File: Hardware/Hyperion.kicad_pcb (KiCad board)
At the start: 2 copper layers, 90.2 x 95.9 mm, 1 part, among them J1 CUBESAT-BUS

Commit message: Add core components
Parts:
- added C1: 3.3uF, CAPC1608, F.Cu at (152.4, 87.6)
- added C10: 1000pF, CAPC1608, F.Cu at (141.0, 97.2)
- added C11: 0.1uF, CAPC1608, F.Cu at (139.1, 97.2)
- added C2: 0.1uF, CAPC1608, F.Cu at (141.0, 94.0)
- added C3: 0.1uF, CAPC1608, F.Cu at (141.0, 102.9)
- added C4: 0.1uF, CAPC1608, F.Cu at (149.2, 110.5)
- added C5: 0.1uF, CAPC1608, F.Cu at (155.6, 110.5)
- added C6: 0.1uF, CAPC1608, F.Cu at (163.8, 102.2)
- added C7: 0.1uF, CAPC1608, F.Cu at (163.8, 97.8)
- added C8: 0.1uF, CAPC1608, F.Cu at (155.6, 87.6)
- added C9: 0.1uF, CAPC1608, F.Cu at (149.2, 87.6)
- added FB1: 10, INDC1608, F.Cu at (139.1, 94.0)
- added U1: TM4C123GH6PZ, QFP50P1600X1600-100N, F.Cu at (152.4, 99.1)
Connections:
- J1 pad 1.1: N-0000092 -> (no net)
- J1 pad 1.10: N-0000070 -> (no net)
- J1 pad 1.11: N-0000065 -> (no net)
- J1 pad 1.12: N-0000060 -> (no net)
- J1 pad 1.13: N-0000055 -> (no net)
- J1 pad 1.14: N-00000103 -> (no net)
- J1 pad 1.15: N-0000099 -> (no net)
- J1 pad 1.16: N-0000095 -> (no net)
- J1 pad 1.17: N-0000091 -> (no net)
- J1 pad 1.18: N-0000087 -> (no net)
- J1 pad 1.19: N-0000083 -> (no net)
- J1 pad 1.2: N-0000078 -> (no net)
- J1 pad 1.20: N-0000069 -> (no net)
- J1 pad 1.21: N-0000064 -> (no net)
- J1 pad 1.22: N-0000059 -> (no net)
- J1 pad 1.23: N-0000054 -> (no net)
- J1 pad 1.24: N-00000102 -> (no net)
- J1 pad 1.25: N-0000098 -> (no net)
- J1 pad 1.26: N-0000094 -> (no net)
- J1 pad 1.27: N-0000090 -> (no net)
- J1 pad 1.28: N-0000086 -> (no net)
- J1 pad 1.29: N-0000082 -> (no net)
- J1 pad 1.3: N-0000077 -> (no net)
- J1 pad 1.30: N-0000068 -> (no net)
- J1 pad 1.31: N-0000063 -> (no net)
- J1 pad 1.32: N-0000058 -> (no net)
- J1 pad 1.33: N-0000066 -> (no net)
- J1 pad 1.34: N-00000101 -> (no net)
- J1 pad 1.35: N-0000097 -> (no net)
- J1 pad 1.36: N-0000093 -> (no net)
- J1 pad 1.37: N-0000089 -> (no net)
- J1 pad 1.38: N-0000085 -> (no net)
- J1 pad 1.39: N-0000081 -> (no net)
- J1 pad 1.4: N-0000076 -> (no net)
- J1 pad 1.40: N-0000067 -> (no net)
- J1 pad 1.41: N-0000062 -> (no net)
- J1 pad 1.42: N-0000057 -> (no net)
- J1 pad 1.43: N-00000104 -> (no net)
- J1 pad 1.44: N-00000100 -> (no net)
- J1 pad 1.45: N-0000096 -> (no net)
- J1 pad 1.46: N-0000079 -> (no net)
- J1 pad 1.47: N-0000088 -> (no net)
- J1 pad 1.48: N-0000084 -> (no net)
- J1 pad 1.49: N-0000080 -> (no net)
- J1 pad 1.5: N-0000075 -> (no net)
- J1 pad 1.50: N-0000053 -> (no net)
- J1 pad 1.51: N-0000061 -> (no net)
- J1 pad 1.52: N-0000056 -> (no net)
- J1 pad 1.6: N-0000074 -> (no net)
- J1 pad 1.7: N-0000073 -> (no net)
- J1 pad 1.8: N-0000072 -> (no net)
- J1 pad 1.9: N-0000071 -> (no net)
- J1 pad 2.1: N-0000040 -> (no net)
- J1 pad 2.10: N-0000018 -> (no net)
- J1 pad 2.11: N-0000013 -> (no net)
- J1 pad 2.12: N-000008 -> (no net)
- J1 pad 2.13: N-000003 -> (no net)
- J1 pad 2.14: N-0000051 -> (no net)
- J1 pad 2.15: N-0000047 -> (no net)
- J1 pad 2.16: N-0000043 -> (no net)
- J1 pad 2.17: N-0000039 -> (no net)
- J1 pad 2.18: N-0000035 -> (no net)
- J1 pad 2.19: N-0000031 -> (no net)
- J1 pad 2.2: N-0000026 -> (no net)
- J1 pad 2.20: N-0000017 -> (no net)
- J1 pad 2.21: N-0000012 -> (no net)
- J1 pad 2.22: N-000007 -> (no net)
- J1 pad 2.23: N-000002 -> (no net)
- J1 pad 2.24: N-0000050 -> (no net)
- J1 pad 2.25: N-0000046 -> (no net)
- J1 pad 2.26: N-0000042 -> (no net)
- J1 pad 2.27: N-0000038 -> (no net)
- J1 pad 2.28: N-0000034 -> (no net)
- J1 pad 2.29: N-0000030 -> (no net)
- J1 pad 2.3: N-0000025 -> (no net)
- J1 pad 2.30: N-0000016 -> (no net)
- J1 pad 2.31: N-0000011 -> (no net)
- J1 pad 2.32: N-000006 -> (no net)
- J1 pad 2.33: N-0000014 -> (no net)
- J1 pad 2.34: N-0000049 -> (no net)
- J1 pad 2.35: N-0000045 -> (no net)
- J1 pad 2.36: N-0000041 -> (no net)
- J1 pad 2.37: N-0000037 -> (no net)
- J1 pad 2.38: N-0000033 -> (no net)
- J1 pad 2.39: N-0000029 -> (no net)
- J1 pad 2.4: N-0000024 -> (no net)
- J1 pad 2.40: N-0000015 -> (no net)
- J1 pad 2.41: N-0000010 -> (no net)
- J1 pad 2.42: N-000005 -> (no net)
- J1 pad 2.43: N-0000052 -> (no net)
- J1 pad 2.44: N-0000048 -> (no net)
- J1 pad 2.45: N-0000044 -> (no net)
- J1 pad 2.46: N-0000027 -> (no net)
- J1 pad 2.47: N-0000036 -> (no net)
- J1 pad 2.48: N-0000032 -> (no net)
- J1 pad 2.49: N-0000028 -> (no net)
- J1 pad 2.5: N-0000023 -> (no net)
- J1 pad 2.50: N-000001 -> (no net)
- J1 pad 2.51: N-000009 -> (no net)
- J1 pad 2.52: N-000004 -> (no net)
- J1 pad 2.6: N-0000022 -> (no net)
- J1 pad 2.7: N-0000021 -> (no net)
- J1 pad 2.8: N-0000020 -> (no net)
- J1 pad 2.9: N-0000019 -> (no net)

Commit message: Core layout
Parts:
- added C12: 0.1uF, CAPC1005-N, F.Cu at (153.8, 113.2)
- added C13: 0.1uF, CAPC1005-N, F.Cu at (158.2, 92.2)
- added C14: 0.1uF, CAPC1005-N, F.Cu at (150.2, 92.2)
- added C15: C, CAPC1005-N, F.Cu at (155.0, 86.8)
- added C16: 0.1uF, CAPC1005-N, F.Cu at (145.2, 98.2)
- added C17: C, CAPC1005-N, F.Cu at (152.5, 86.8)
- added C18: 0.1uF, CAPC1005-N, F.Cu at (145.2, 104.8)
- added R1: 1k, RESC1005-N, F.Cu at (157.0, 86.0)
- added R2: R, RESC1005-N, F.Cu at (152.5, 92.2)
- added X1: 32.768kHz, XTAL-2SMD-32x15, F.Cu at (160.0, 89.5)
- added X2: 16MHz, XTAL-2SMD-50X32, F.Cu at (153.8, 89.5)
- C1: value 3.3uF -> 0.1uF; footprint CAPC1608 -> CAPC1005-N
- C10: value 1000pF -> 0.1uF; footprint CAPC1608 -> CAPC1005-N
- C11, C8: value 0.1uF -> 20pF; footprint CAPC1608 -> CAPC1005-N
- C2, C3, C4, C5, C7: footprint CAPC1608 -> CAPC1005-N
- C6: value 0.1uF -> 3.3uF; footprint CAPC1608 -> CAPC1005-N
- C9: value 0.1uF -> 1000pF; footprint CAPC1608 -> CAPC1005-N
- FB1: footprint INDC1608 -> INDC1005-N
- moved C9 24.5 mm to (153.8, 111.8), turned to 0 degrees
- moved C10 23.8 mm to (164.8, 98.8), turned to 90 degrees
- moved FB1 22.8 mm to (151.2, 113.2), turned to 180 degrees
- moved C11 22.3 mm to (158.8, 86.8), turned to 0 degrees
- moved C2 20.5 mm to (151.2, 111.8), turned to 0 degrees
- moved C6 20.1 mm to (143.8, 101.2), turned to 270 degrees
- moved C1 18.8 mm to (164.8, 101.8), turned to 90 degrees
- moved C3 18.2 mm to (155.8, 92.2), turned to 180 degrees
- moved C4 10.1 mm to (145.2, 101.2), turned to 270 degrees
- moved C7 7.02 mm to (164.8, 104.8), turned to 90 degrees
- moved C8 5.74 mm to (161.2, 86.8)
- moved J1 4.27 mm to (110.0, 150.0)
- moved U1 3.92 mm to (155.0, 102.0)
- moved C5 3.42 mm to (158.8, 111.8)
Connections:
- C1 pad 1: N-00000105 -> N-00000153
- C10 pad 1: N-00000109 -> +3.3VDAC
- C10 pad 2: GNDA -> GND
- C11 pad 1: N-00000109 -> /Core/XOSC1
- C11 pad 2: GNDA -> /Core/GNDX
- C2 pad 1: +3.3V -> +3.3VDAC
- C3 pad 1: +3.3V -> /Core/~RST
- C4 pad 1: +3.3V -> N-00000153
- C5 pad 1: +3.3V -> +3.3VDAC
- C6 pad 1: +3.3V -> N-00000153
- C7 pad 1: +3.3V -> +3.3VDAC
- C8 pad 1: +3.3V -> /Core/XOSC0
- C8 pad 2: GND -> /Core/GNDX
- C9 pad 1: +3.3V -> +3.3VADC
- FB1 pad 1: N-00000109 -> +3.3VADC
- FB1 pad 2: +3.3V -> +3.3VDAC
- J1 pad 2.25: (no net) -> +5V
- J1 pad 2.26: (no net) -> +5V
- J1 pad 2.27: (no net) -> +3.3V
- J1 pad 2.28: (no net) -> +3.3V
- J1 pad 2.29: (no net) -> DGND
- J1 pad 2.30: (no net) -> DGND
- J1 pad 2.32: (no net) -> DGND
- J1 pad 2.45: (no net) -> +BATT
- J1 pad 2.46: (no net) -> +BATT
- U1 pad 10: GNDA -> GND
- U1 pad 20: +3.3V -> +3.3VDAC
- U1 pad 32: +3.3V -> +3.3VDAC
- U1 pad 38: N-00000105 -> N-00000153
- U1 pad 44: +3.3V -> +3.3VDAC
- U1 pad 5: +3.3V -> +3.3VDAC
- U1 pad 52: (no net) -> /Core/XOSC0
- U1 pad 53: (no net) -> /Core/GNDX
- U1 pad 54: (no net) -> /Core/XOSC1
- U1 pad 56: +3.3V -> +3.3VDAC
- U1 pad 63: (no net) -> /Core/~RST
- U1 pad 65: (no net) -> /Core/OSC0
- U1 pad 66: (no net) -> /Core/OSC1
- U1 pad 67: +3.3V -> +3.3VDAC
- U1 pad 7: N-00000109 -> +3.3VADC
- U1 pad 80: +3.3V -> +3.3VDAC
- U1 pad 82: (no net) -> /Core/TDO
- U1 pad 83: (no net) -> /Core/TDI
- U1 pad 84: (no net) -> /Core/TMS
- U1 pad 85: (no net) -> /Core/TCK
- U1 pad 86: N-00000105 -> N-00000153
- U1 pad 93: +3.3V -> +3.3VDAC
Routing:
- net GND: track 0.00 -> 43.0 mm, vias 0 -> 13
- net +3.3VDAC: track 0.00 -> 32.8 mm, vias 0 -> 8
- net N-00000153: track 0.00 -> 21.6 mm
- net /Core/OSC0: track 0.00 -> 9.17 mm
- net /Core/GNDX: track 0.00 -> 9.15 mm
- net /Core/XOSC1: track 0.00 -> 8.05 mm
- net /Core/XOSC0: track 0.00 -> 8.05 mm
- net +3.3VADC: track 0.00 -> 6.16 mm
- net N-0000089: track 0.00 -> 5.77 mm
- net /Core/~RST: track 0.00 -> 4.54 mm, vias 0 -> 1
- net /Core/OSC1: track 0.00 -> 2.28 mm
- added copper zone on Inner2.Cu, net +3.3VDAC
- added copper zone on Inner1.Cu, net GND
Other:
- board outline removed
- copper layers 2 -> 4
- net class Default: clearance 0.254 -> 0.2032; trace_width 0.254 -> 0.2032; via_dia 0.889 -> 0.762; via_drill 0.635 -> 0.381
- rule trace_clearance: 0.254 -> 0.2032
- rule trace_min: 0.254 -> 0.2032
- rule via_min_drill: 0.508 -> 0.381
- rule via_min_size: 0.889 -> 0.635

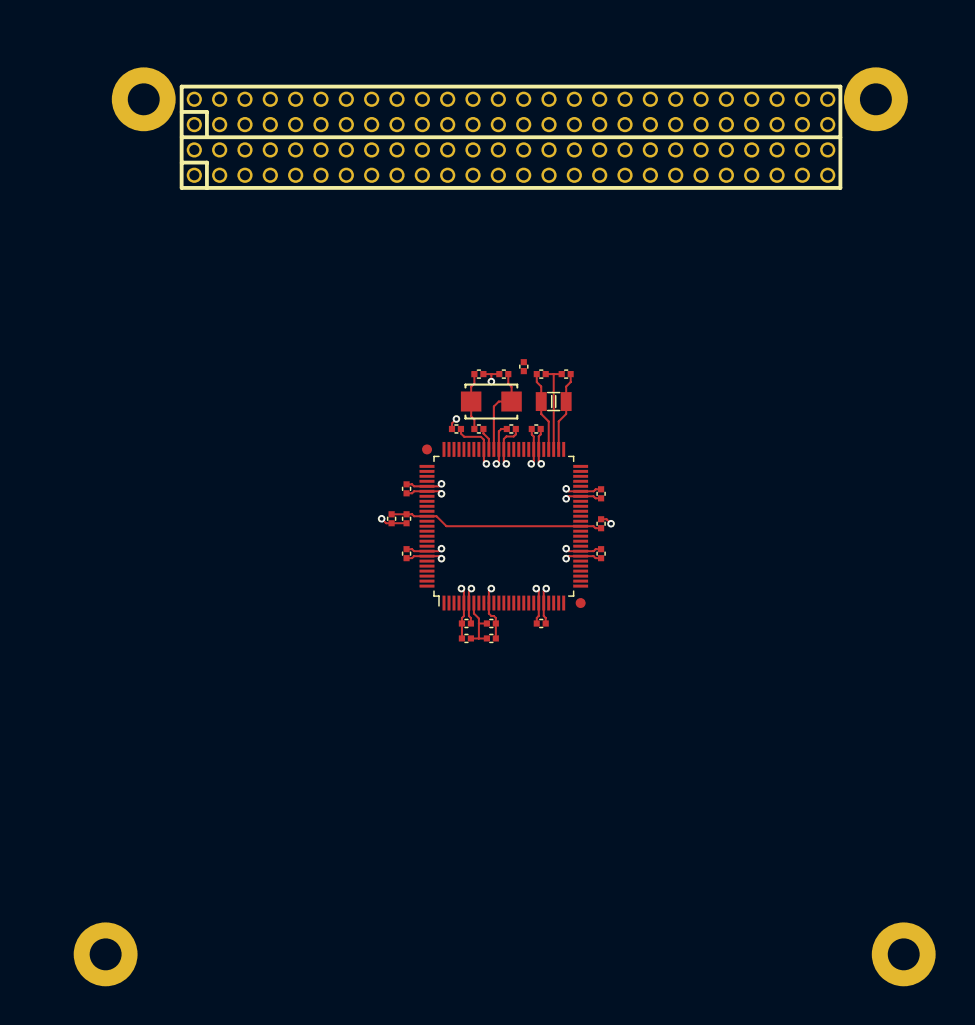
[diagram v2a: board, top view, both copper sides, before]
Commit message: Add dual channel FTDI
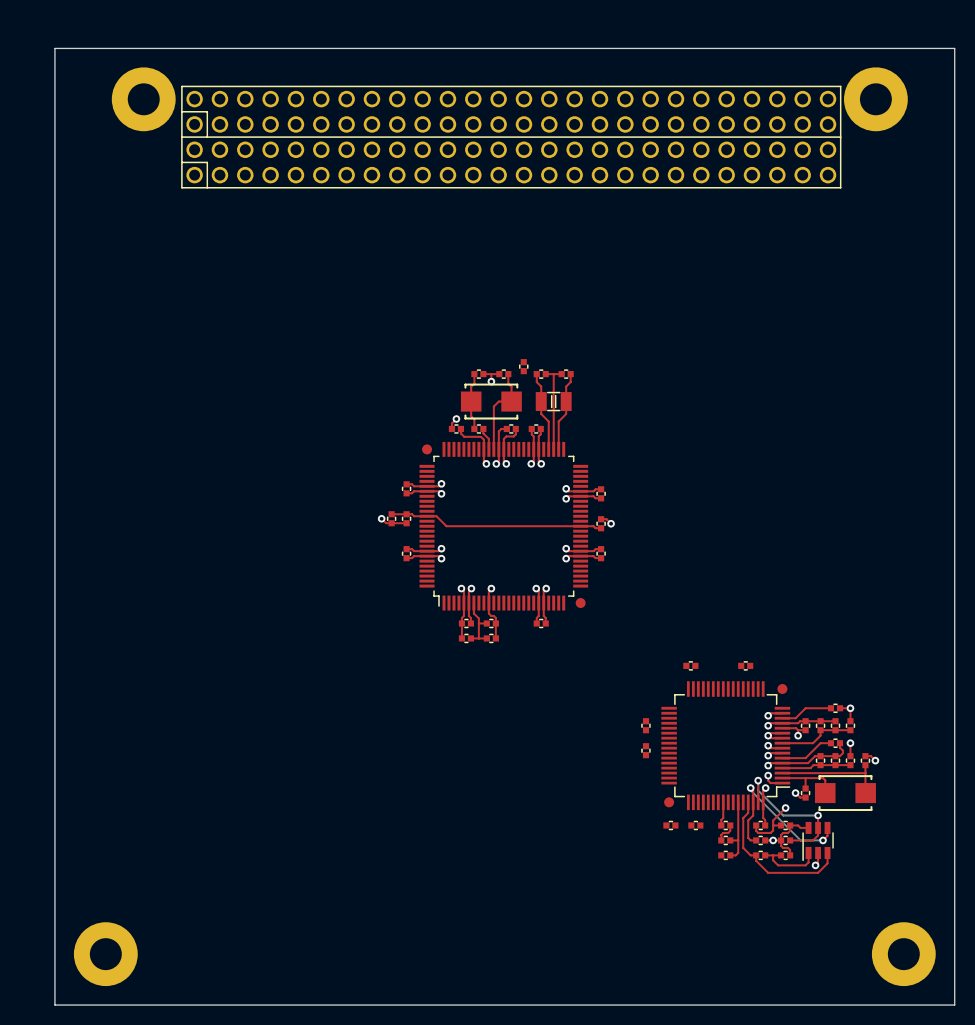
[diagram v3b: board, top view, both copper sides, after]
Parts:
- added C19: 0.1uF, CAPC1005-N, F.Cu at (179.2, 116.0)
- added C20: 3.3uF, CAPC1005-N, F.Cu at (171.8, 132.0)
- added C21: 0.1uF, CAPC1005-N, F.Cu at (173.8, 116.0)
- added C22: 0.1uF, CAPC1005-N, F.Cu at (185.2, 122.0)
- added C23: 0.1uF, CAPC1005-N, F.Cu at (169.2, 124.5)
- added C24: 0.1uF, CAPC1005-N, F.Cu at (169.2, 122.0)
- added C25: 0.1uF, CAPC1005-N, F.Cu at (177.2, 132.0)
- added C26: 0.1uF, CAPC1005-N, F.Cu at (180.8, 132.0)
- added C27: 3.3uF, CAPC1005-N, F.Cu at (188.2, 122.0)
- added C28: 0.1uF, CAPC1005-N, F.Cu at (186.8, 122.0)
- added C29: 3.3uF, CAPC1005-N, F.Cu at (188.2, 125.5)
- added C30: 0.1uF, CAPC1005-N, F.Cu at (186.8, 125.5)
- added C31: C, CAPC1005-N, F.Cu at (185.2, 128.8)
- added C32: C, CAPC1005-N, F.Cu at (191.2, 125.5)
- added C33: 0.1uF, CAPC1005-N, F.Cu at (183.2, 132.0)
- added C34: 0.1uF, CAPC1005-N, F.Cu at (174.2, 132.0)
- added FB2: FERRITE, INDC1005-N, F.Cu at (189.8, 122.0)
- added FB3: FERRITE, INDC1005-N, F.Cu at (189.8, 125.5)
- added R10: R, RESC1005-N, F.Cu at (180.8, 135.0)
- added R3: R, RESC1005-N, F.Cu at (188.2, 120.2)
- added R4: R, RESC1005-N, F.Cu at (188.2, 123.8)
- added R5: R, RESC1005-N, F.Cu at (177.2, 135.0)
- added R6: R, RESC1005-N, F.Cu at (177.2, 133.5)
- added R7: R, RESC1005-N, F.Cu at (183.2, 135.0)
- added R8: R, RESC1005-N, F.Cu at (183.2, 133.5)
- added R9: R, RESC1005-N, F.Cu at (180.8, 133.5)
- added U2: FT2232H, QFP50P1200X1200-64N, F.Cu at (177.2, 124.0)
- added U3: 93LC46/OT, SOT95P280-6N, F.Cu at (186.5, 133.5)
- added X3: CRYSTAL, XTAL-2SMD-50X32, F.Cu at (189.2, 128.8)
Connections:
- J1 pad 2.33: (no net) -> /Bus/S0
- J1 pad 2.34: (no net) -> /Bus/S0
- J1 pad 2.35: (no net) -> /Bus/S1
- J1 pad 2.36: (no net) -> /Bus/S1
- J1 pad 2.37: (no net) -> /Bus/S2
- J1 pad 2.38: (no net) -> /Bus/S2
- J1 pad 2.39: (no net) -> /Bus/S3
- J1 pad 2.40: (no net) -> /Bus/S3
- J1 pad 2.41: (no net) -> /Bus/S4
- J1 pad 2.42: (no net) -> /Bus/S4
- J1 pad 2.43: (no net) -> /Bus/S5
- J1 pad 2.44: (no net) -> /Bus/S5
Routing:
- net GND: track 43.0 -> 77.6 mm, vias 13 -> 22
- net N-00000139: track 0.00 -> 17.2 mm, vias 0 -> 2
- net N-00000140: track 0.00 -> 16.0 mm
- net N-00000149: track 0.00 -> 15.2 mm, vias 0 -> 2
- net +3.3VDAC: track 32.8 -> 46.8 mm, vias 8 -> 11
- net /Access/OSCO: track 0.00 -> 11.1 mm
- net N-00000137: track 0.00 -> 7.68 mm
- net N-00000136: track 0.00 -> 6.94 mm
- net N-00000141: track 0.00 -> 6.93 mm
- net +1.8V: track 0.00 -> 6.89 mm, vias 0 -> 2
- net N-00000146: track 0.00 -> 6.77 mm
- net /Access/OSCI: track 0.00 -> 6.71 mm
- net N-00000147: track 0.00 -> 5.49 mm
- net N-00000150: track 0.00 -> 5.28 mm
- net N-00000145: track 0.00 -> 1.53 mm, vias 0 -> 1
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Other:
- board outline added: 90.2 x 95.9 mm
